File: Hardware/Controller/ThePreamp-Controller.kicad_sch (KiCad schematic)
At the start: 22 parts, among them J1 8V, J2 Power relay trigger, J3 SPI DISPLAY 1, J4 SPI DISPLAY 2, J5 Digital Out, J6 3.3V (Opt), J8 12V, SW1 RotaryEncoder_Switch, SW2 RotaryEncoder_Switch, U1 TSOP34838, U2 CAT24C64WI-GT3, U3 ESP32-DEVKIT-V1, U4 APC-817B1-SL

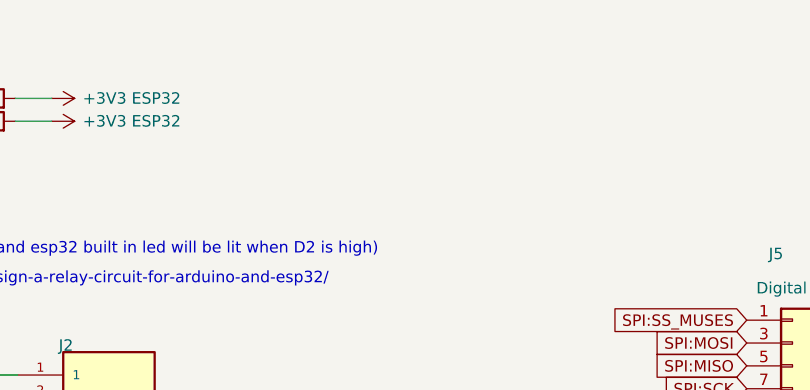
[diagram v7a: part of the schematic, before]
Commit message: Added pullup resistors on D34-35 on controller pcb
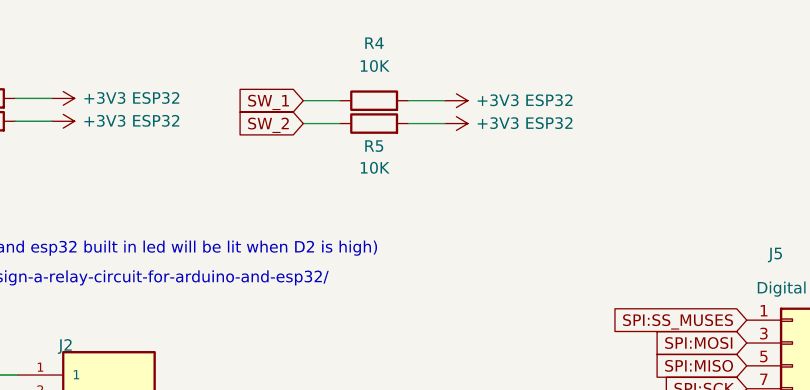
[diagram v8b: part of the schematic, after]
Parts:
- added R4, R5: 10K, Resistor_SMD:R_0805_2012Metric_Pad1.20x1.40mm_HandSolder, symbol Device:R
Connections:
- net +3V3 ESP32: now also R4.2, R5.2
- net SW_1: now also R4.1
- net SW_2: now also R5.1
